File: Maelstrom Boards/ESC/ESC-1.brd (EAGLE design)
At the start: 101.6 x 101.6 mm, 27 parts

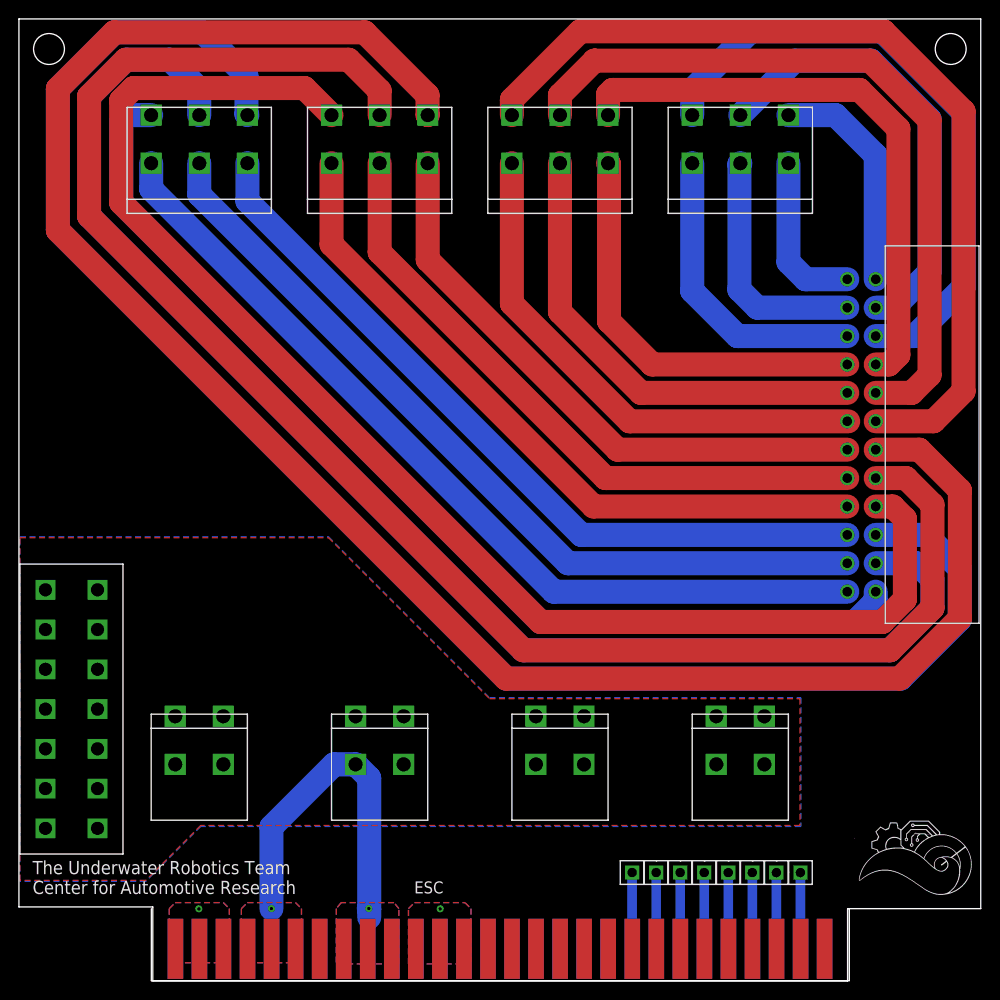
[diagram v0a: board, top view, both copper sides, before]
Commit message: Created new vertical connector, updated 24 pin connector, mostly done with routing.
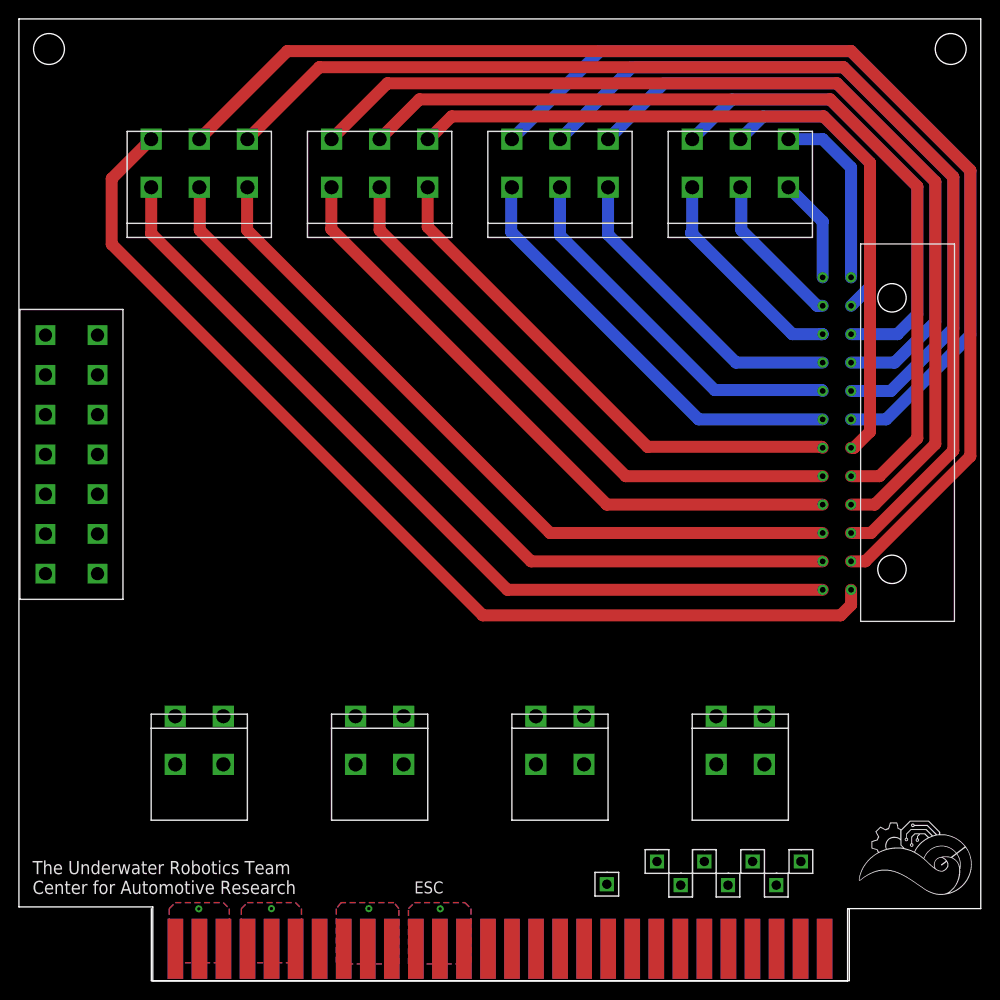
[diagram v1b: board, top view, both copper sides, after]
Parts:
- moved U$19 26.9 mm to (2.80, 43.0)
- moved U$20 2.94 mm to (62.1, 10.2), turned to 0 degrees
- moved U$18 2.61 mm to (84.9, 41.3)
- moved 1 2.54 mm to (76.2, 83.8)
- moved 3 2.54 mm to (57.1, 83.8)
- moved 5 2.54 mm to (38.1, 83.8)
- moved 7 2.54 mm to (19.1, 83.8)
- moved 2 2.54 mm to (76.2, 88.9)
- moved 4 2.54 mm to (57.1, 88.9)
- moved 6 2.54 mm to (38.1, 88.9)
- moved 8 2.54 mm to (19.1, 88.9)
- moved U$22 1.33 mm to (69.9, 10.1)
- moved U$24 1.33 mm to (74.9, 10.1)
- moved U$26 1.33 mm to (80.0, 10.1)
- moved U$21 1.17 mm to (67.4, 12.6)
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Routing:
- net N$16: track 203.1 -> 80.8 mm
- net N$18: track 176.9 -> 97.6 mm
- net N$24: track 176.6 -> 125.8 mm
- net N$17: track 149.0 -> 109.8 mm
- net GND: track 37.1 -> 0.00 mm
- net N$4: track 67.3 -> 50.7 mm
- net N$5: track 48.3 -> 32.7 mm
- net N$23: track 149.6 -> 137.9 mm
- net N$7: track 43.8 -> 33.3 mm
- net N$8: track 49.6 -> 39.6 mm
- net N$9: track 55.5 -> 45.9 mm
- net N$2: track 25.6 -> 16.5 mm
- net N$3: track 31.8 -> 23.4 mm
- net PWM_1: track 9.06 -> 0.98 mm
- net PWM_8: track 8.11 -> 0.05 mm
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- removed copper zone on layer 1, net BALANCED+
